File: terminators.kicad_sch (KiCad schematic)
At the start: 13 parts, among them U37 74LS32

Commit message: more work on BOM done
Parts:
- R191, R192: MFG Name (none) -> YAGEO; MFG Part Num (none) -> MFR-25FBF52-1K; Mouser (none) -> 603-MFR-25FBF52-1K
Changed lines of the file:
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@@
 			)
 		)
-		(property "Mouser" ""
+		(property "Mouser" "603-MFR-25FBF52-1K "
+			(at 76.073 164.719 90)
+			(effects
+				(font
+					(size 1.27 1.27)
+				)
+				(hide yes)
+			)
+		)
+		(property "MFG Name" "YAGEO"
+			(at 76.073 164.719 90)
+			(effects
+				(font
+					(size 1.27 1.27)
+				)
+				(hide yes)
+			)
+		)
+		(property "MFG Part Num" "MFR-25FBF52-1K"
 			(at 76.073 164.719 90)
 			(effects
@@
 			)
 		)
-		(property "Mouser" ""
+		(property "Mouser" "603-MFR-25FBF52-1K "
 			(at 76.073 169.291 90)
 			(effects
+				(font
+					(size 1.27 1.27)
+				)
+				(hide yes)
+			)
+		)
+		(property "MFG Name" "YAGEO"
+			(at 76.073 169.291 90)
+			(effects
+				(font
+					(size 1.27 1.27)
+				)
+				(hide yes)
+			)
+		)
+		(property "MFG Part Num" "MFR-25FBF52-1K"
+			(at 76.073 169.291 90)
+			(effects

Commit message: BOM updates
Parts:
- RP101, RP102: MFG Name (none) -> BOURNS; MFG Part Num (none) -> 4610X-101-472LF; Mouser (none) -> 652-4610X-1LF-4.7K
- RP104: MFG Name (none) -> BOURNS; MFG Part Num (none) -> 4610X-101-471LF; Mouser (none) -> 652-4610X-1LF-470
- U37: MFG Part Num SN74LS32N -> SN74LS32N; Mouser (none) -> 595-SN74LS32N
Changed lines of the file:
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@@
 			)
 		)
-		(property "Mouser" ""
+		(property "Mouser" "652-4610X-1LF-4.7K"
+			(at 91.694 129.159 90)
+			(effects
+				(font
+					(size 1.27 1.27)
+				)
+				(hide yes)
+			)
+		)
+		(property "MFG Name" "BOURNS"
+			(at 91.694 129.159 90)
+			(effects
+				(font
+					(size 1.27 1.27)
+				)
+				(hide yes)
+			)
+		)
+		(property "MFG Part Num" "4610X-101-472LF "
 			(at 91.694 129.159 90)
 			(effects
@@
 			)
 		)
-		(property "Mouser" ""
+		(property "Mouser" "652-4610X-1LF-4.7K"
+			(at 160.02 129.286 90)
+			(effects
+				(font
+					(size 1.27 1.27)
+				)
+				(hide yes)
+			)
+		)
+		(property "MFG Name" "BOURNS"
+			(at 160.02 129.286 90)
+			(effects
+				(font
+					(size 1.27 1.27)
+				)
+				(hide yes)
+			)
+		)
+		(property "MFG Part Num" "4610X-101-472LF "
 			(at 160.02 129.286 90)
 			(effects
@@
 			)
 		)
-		(property "Mouser" ""
+		(property "Mouser" "652-4610X-1LF-470 "
+			(at 160.02 164.719 90)
+			(effects
+				(font
+					(size 1.27 1.27)
+				)
+				(hide yes)
+			)
+		)
+		(property "MFG Name" "BOURNS"
+			(at 160.02 164.719 90)
+			(effects
+				(font
+					(size 1.27 1.27)
+				)
+				(hide yes)
+			)
+		)
+		(property "MFG Part Num" "4610X-101-471LF "
 			(at 160.02 164.719 90)
 			(effects
@@
 			)
 		)
-		(property "MFG Part Num" "SN74LS32N"
+		(property "MFG Part Num" "SN74LS32N "
 			(at 219.964 132.207 0)
 			(effects
@@
 			)
 		)
-		(property "Mouser" ""
+		(property "Mouser" "595-SN74LS32N "
 			(at 219.964 132.207 0)
 			(effects
@@
 			)
 		)
-		(property "MFG Part Num" "SN74LS32N"
+		(property "MFG Part Num" "SN74LS32N "
 			(at 244.475 144.272 0)
 			(effects
@@
 			)
 		)
-		(property "Mouser" ""
+		(property "Mouser" "595-SN74LS32N "
 			(at 244.475 144.272 0)
 			(effects

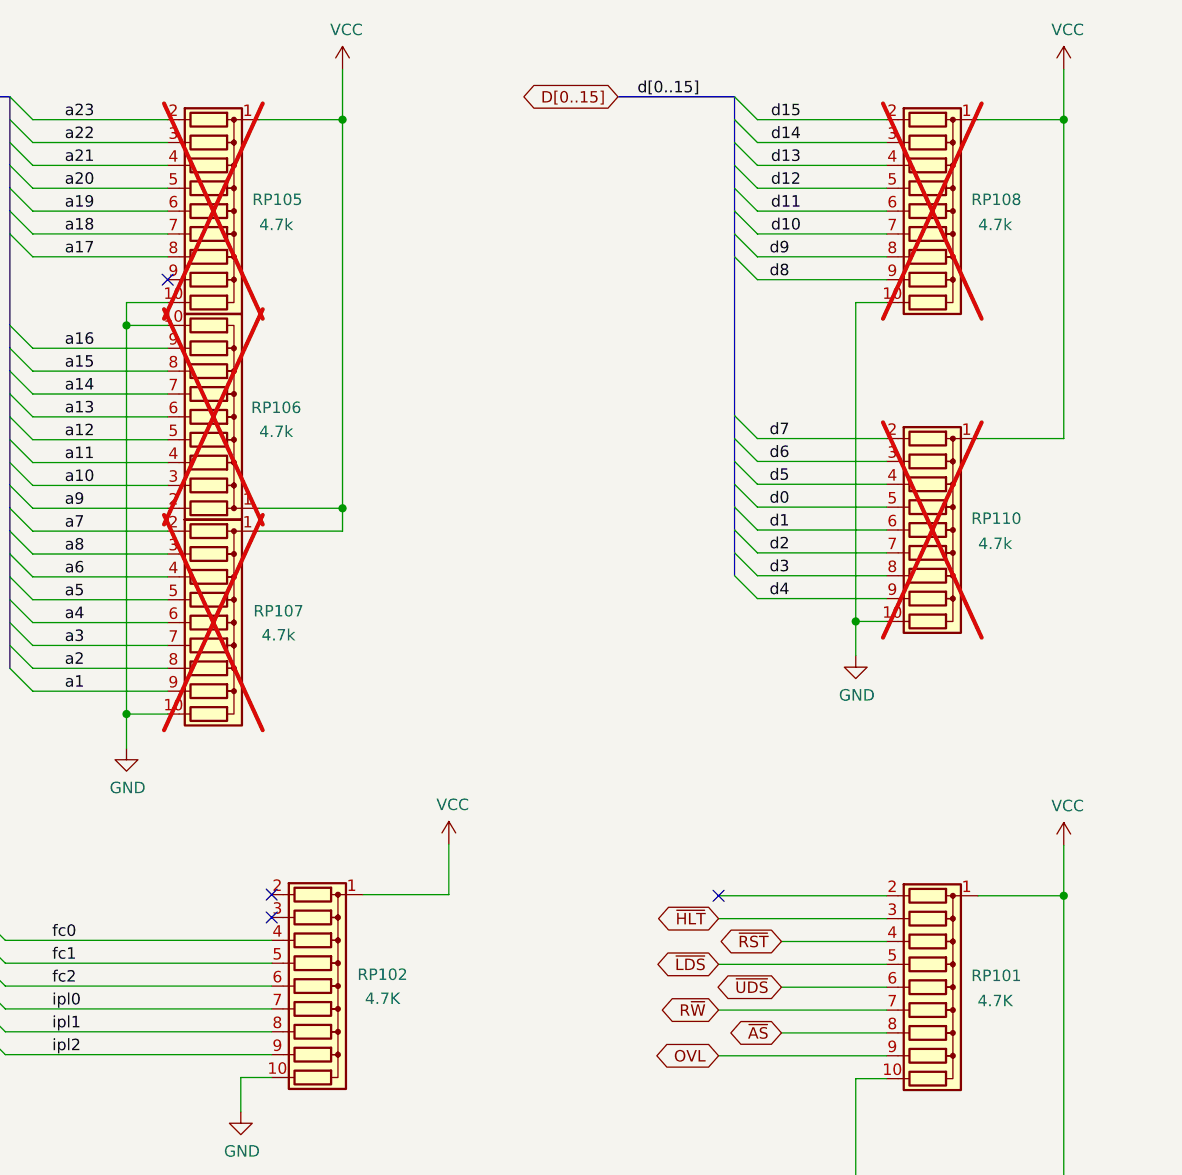
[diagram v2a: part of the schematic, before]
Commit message: replaced commodore hybrid with OpenAmigaVideoHybrid
decided to place address pullups for better EPROM capability
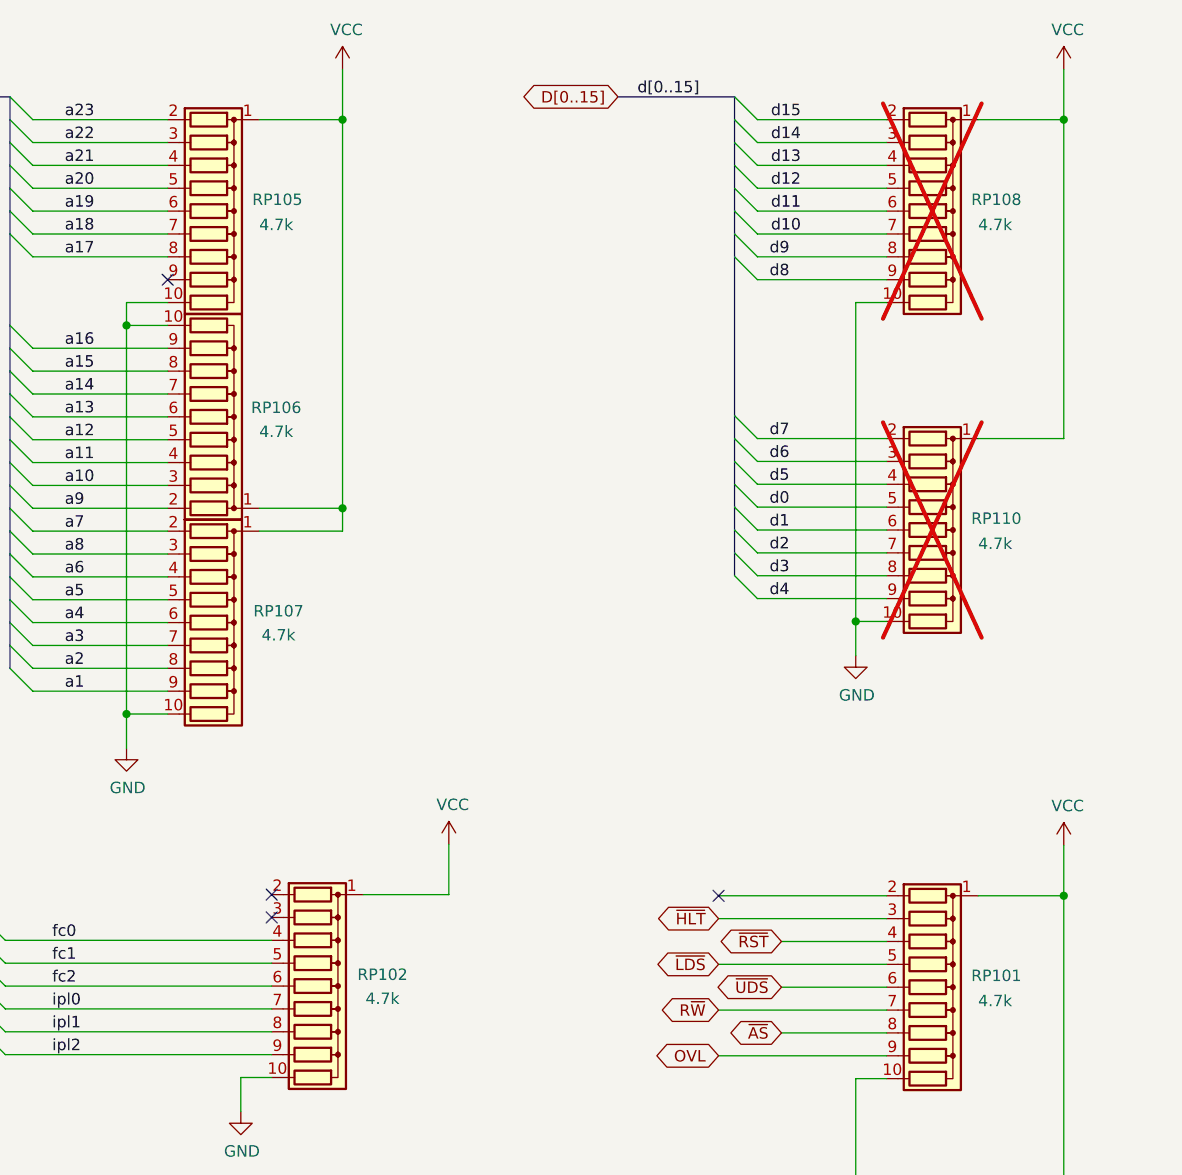
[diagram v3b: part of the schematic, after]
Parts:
- RP101, RP102: value 4.7K -> 4.7k
- RP105, RP106, RP107: MFG Name (none) -> BOURNS; MFG Part Num (none) -> 4610X-101-472LF; Mouser (none) -> 652-4610X-1LF-4.7K; now fitted
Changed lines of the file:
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@@
 		(in_bom yes)
 		(on_board yes)
-		(dnp yes)
+		(dnp no)
 		(property "Reference" "RP107"
 			(at 87.376 87.503 90)
@@
 			)
 		)
-		(property "Mouser" ""
+		(property "Mouser" "652-4610X-1LF-4.7K"
+			(at 80.137 88.773 90)
+			(effects
+				(font
+					(size 1.27 1.27)
+				)
+				(hide yes)
+			)
+		)
+		(property "MFG Name" "BOURNS"
+			(at 80.137 88.773 90)
+			(effects
+				(font
+					(size 1.27 1.27)
+				)
+				(hide yes)
+			)
+		)
+		(property "MFG Part Num" "4610X-101-472LF "
 			(at 80.137 88.773 90)
 			(effects
@@
 		(in_bom yes)
 		(on_board yes)
-		(dnp yes)
+		(dnp no)
 		(property "Reference" "RP106"
 			(at 87.122 64.897 90)
@@
 			)
 		)
-		(property "Mouser" ""
+		(property "Mouser" "652-4610X-1LF-4.7K"
+			(at 80.137 65.913 90)
+			(effects
+				(font
+					(size 1.27 1.27)
+				)
+				(hide yes)
+			)
+		)
+		(property "MFG Name" "BOURNS"
+			(at 80.137 65.913 90)
+			(effects
+				(font
+					(size 1.27 1.27)
+				)
+				(hide yes)
+			)
+		)
+		(property "MFG Part Num" "4610X-101-472LF "
 			(at 80.137 65.913 90)
 			(effects
@@
 		(in_bom yes)
 		(on_board yes)
-		(dnp yes)
+		(dnp no)
 		(property "Reference" "RP105"
 			(at 87.249 41.783 90)
@@
 			)
 		)
-		(property "Mouser" ""
+		(property "Mouser" "652-4610X-1LF-4.7K"
+			(at 80.137 43.053 90)
+			(effects
+				(font
+					(size 1.27 1.27)
+				)
+				(hide yes)
+			)
+		)
+		(property "MFG Name" "BOURNS"
+			(at 80.137 43.053 90)
+			(effects
+				(font
+					(size 1.27 1.27)
+				)
+				(hide yes)
+			)
+		)
+		(property "MFG Part Num" "4610X-101-472LF "
 			(at 80.137 43.053 90)
 			(effects
@@
 			)
 		)
-		(property "Value" "4.7K"
+		(property "Value" "4.7k"
 			(at 98.933 130.556 90)
 			(effects
@@
 			)
 		)
-		(property "Value" "4.7K"
+		(property "Value" "4.7k"
 			(at 167.005 130.81 90)
 			(effects

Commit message: more silkscreen work
removed sockets for standard IC's
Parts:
- U37: footprint Package_DIP:DIP-14_W7.62mm_Socket_LongPads -> Package_DIP:DIP-14_W7.62mm_LongPads
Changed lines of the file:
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@@
 	(title_block
 		(title "Rämixx500_max")
-		(date "2026-04-09")
+		(date "2026-04-26")
 		(rev "3")
 		(company "SukkoPera")
@@
 			)
 		)
-		(property "Footprint" "Package_DIP:DIP-14_W7.62mm_Socket_LongPads"
+		(property "Footprint" "Package_DIP:DIP-14_W7.62mm_LongPads"
 			(at 219.964 132.207 0)
 			(effects
@@
 			)
 		)
-		(property "Footprint" "Package_DIP:DIP-14_W7.62mm_Socket_LongPads"
+		(property "Footprint" "Package_DIP:DIP-14_W7.62mm_LongPads"
 			(at 244.475 144.272 0)
 			(effects
